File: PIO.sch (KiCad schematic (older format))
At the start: 12 parts, among them J1 Conn_02x08_Odd_Even, J2 KMDGX-6S-BS, U15 Z84C20, U16 74AHC08, U18 74HC164, U19 74HC164, U2 74AHC14

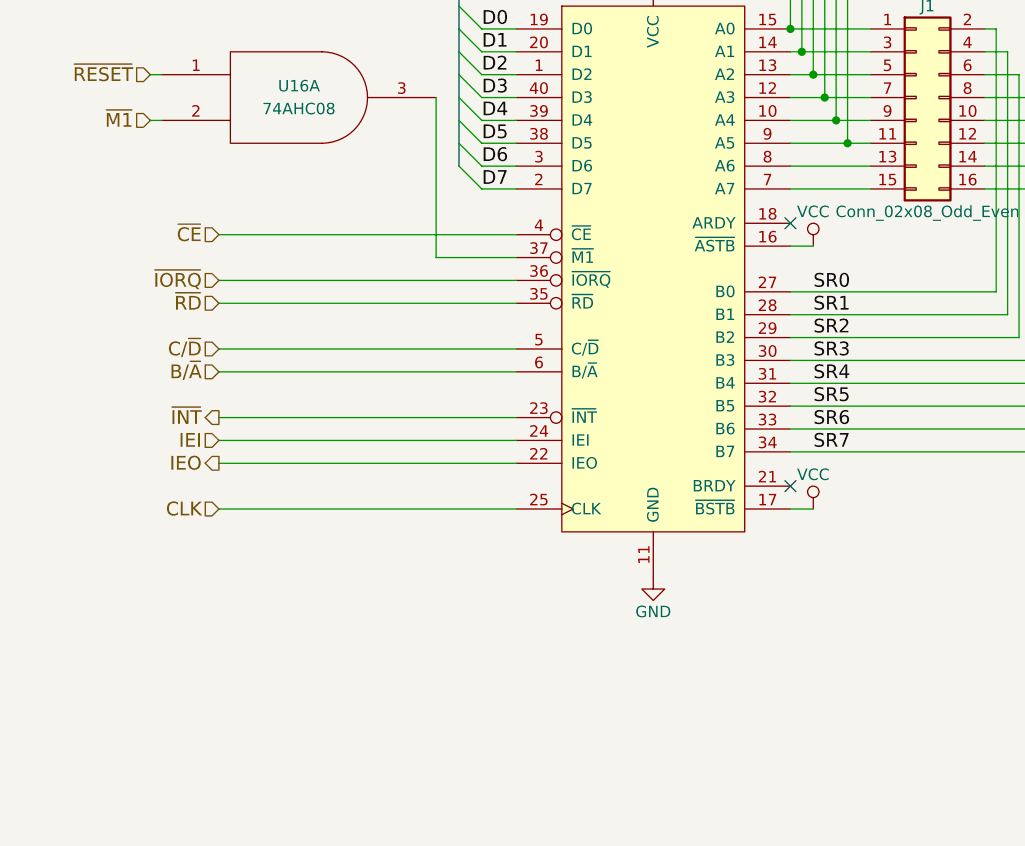
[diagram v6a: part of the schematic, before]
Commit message: Schematic for an LCD panel interface circuit.
git-svn-id: svn+ssh://dev.thehead.ca/depot/main/z80@632 995eaefb-0ce2-40e3-b8bc-69bf8729875b
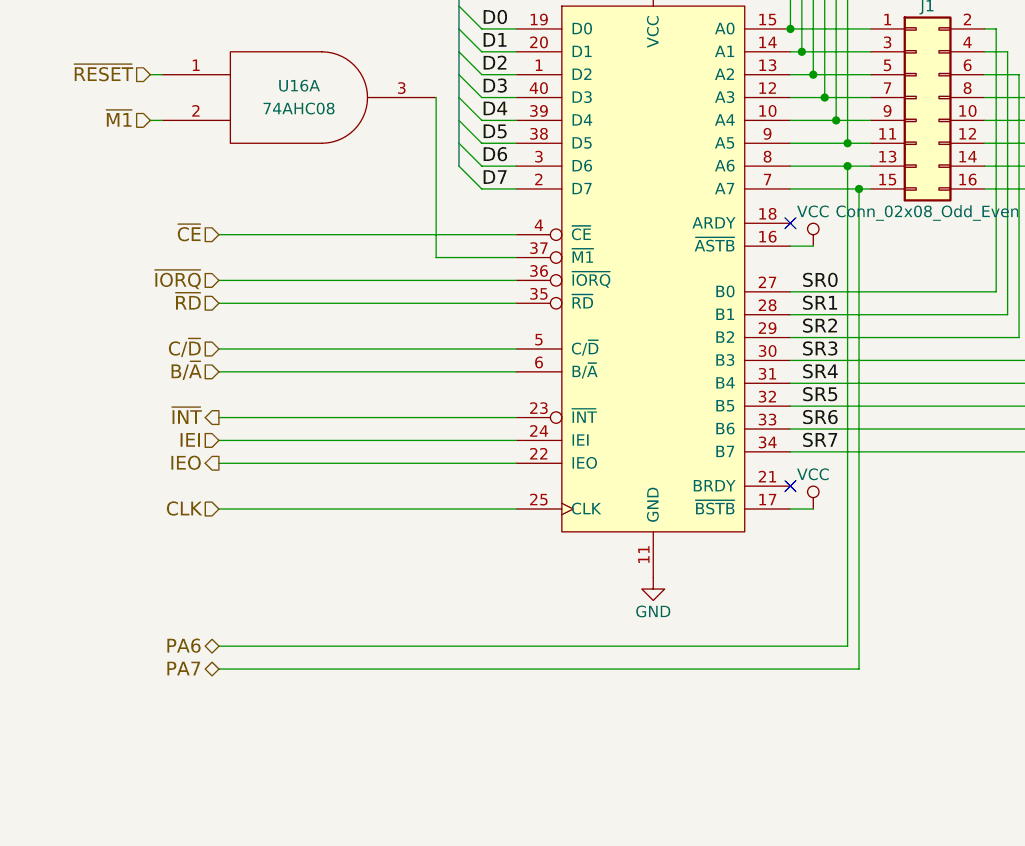
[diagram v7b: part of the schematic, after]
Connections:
- net PA7: now reaches J1.15 (Pin_15), U15.7 (A7)
- net PA6: now reaches J1.13 (Pin_13), U15.8 (A6)
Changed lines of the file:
@@
 $Descr USLetter 11000 8500
 encoding utf-8
-Sheet 5 7
+Sheet 5 8
 Title "PIO, PS/2 Keyboard Port"
-Date "2018-06-12"
-Rev "10"
+Date "2018-07-18"
+Rev "11"
 Comp ""
 Comment1 ""
@@
 ~RESET
 $Comp
-L GND #PWR055
+L GND #PWR057
 U 1 1 59D82A6F
 P 3400 4500
-F 0 "#PWR055" H 3400 4250 50  0001 C CNN
+F 0 "#PWR057" H 3400 4250 50  0001 C CNN
 F 1 "GND" H 3400 4350 50  0000 C CNN
 F 2 "" H 3400 4500 50  0001 C CNN
@@
 $EndComp
 $Comp
-L VCC #PWR056
+L VCC #PWR058
 U 1 1 59D82A86
 P 3400 1800
-F 0 "#PWR056" H 3400 1650 50  0001 C CNN
+F 0 "#PWR058" H 3400 1650 50  0001 C CNN
 F 1 "VCC" H 3400 1950 50  0000 C CNN
 F 2 "" H 3400 1800 50  0001 C CNN
@@
 NoConn ~ 4000 4100
 $Comp
-L VCC #PWR057
+L VCC #PWR059
 U 1 1 59D87E9E
 P 4100 3050
-F 0 "#PWR057" H 4100 2900 50  0001 C CNN
+F 0 "#PWR059" H 4100 2900 50  0001 C CNN
 F 1 "VCC" H 4100 3200 50  0000 C CNN
 F 2 "" H 4100 3050 50  0001 C CNN
@@
 $EndComp
 $Comp
-L VCC #PWR058
+L VCC #PWR060
 U 1 1 59D87EBB
 P 4100 4200
-F 0 "#PWR058" H 4100 4050 50  0001 C CNN
+F 0 "#PWR060" H 4100 4050 50  0001 C CNN
 F 1 "VCC" H 4100 4350 50  0000 C CNN
 F 2 "" H 4100 4200 50  0001 C CNN
@@
 	4000 3950 5250 3950
 $Comp
-L VCC #PWR059
+L VCC #PWR061
 U 1 1 59D89429
 P 9400 1200
-F 0 "#PWR059" H 9400 1050 50  0001 C CNN
+F 0 "#PWR061" H 9400 1050 50  0001 C CNN
 F 1 "VCC" H 9400 1350 50  0000 C CNN
 F 2 "" H 9400 1200 50  0001 C CNN
@@
 $EndComp
 $Comp
-L GND #PWR060
+L GND #PWR062
 U 1 1 59D8949E
 P 10200 1200
-F 0 "#PWR060" H 10200 950 50  0001 C CNN
+F 0 "#PWR062" H 10200 950 50  0001 C CNN
 F 1 "GND" H 10200 1050 50  0000 C CNN
 F 2 "" H 10200 1200 50  0001 C CNN
@@
 $EndComp
 $Comp
-L VCC #PWR061
+L VCC #PWR063
 U 1 1 59D8DE5C
 P 9650 2550
-F 0 "#PWR061" H 9650 2400 50  0001 C CNN
+F 0 "#PWR063" H 9650 2400 50  0001 C CNN
 F 1 "VCC" H 9650 2700 50  0000 C CNN
 F 2 "" H 9650 2550 50  0001 C CNN
@@
 $EndComp
 $Comp
-L VCC #PWR062
+L VCC #PWR064
 U 1 1 59D8DE9B
 P 9650 1850
-F 0 "#PWR062" H 9650 1700 50  0001 C CNN
+F 0 "#PWR064" H 9650 1700 50  0001 C CNN
 F 1 "VCC" H 9650 2000 50  0000 C CNN
 F 2 "" H 9650 1850 50  0001 C CNN
@@
 $EndComp
 $Comp
-L GND #PWR063
+L GND #PWR065
 U 1 1 59D929E0
 P 4450 6850
-F 0 "#PWR063" H 4450 6600 50  0001 C CNN
+F 0 "#PWR065" H 4450 6600 50  0001 C CNN
 F 1 "GND" H 4450 6700 50  0000 C CNN
 F 2 "" H 4450 6850 50  0001 C CNN
@@
 $EndComp
 $Comp
-L VCC #PWR064
+L VCC #PWR066
 U 1 1 59D929ED
 P 4450 6550
-F 0 "#PWR064" H 4450 6400 50  0001 C CNN
+F 0 "#PWR066" H 4450 6400 50  0001 C CNN
 F 1 "VCC" H 4450 6700 50  0000 C CNN
 F 2 "" H 4450 6550 50  0001 C CNN
@@
 Text Label 6450 3500 0    60   ~ 0
 SR0
-Text Label 4100 3250 0    60   ~ 0
+Text Label 4050 3250 0    60   ~ 0
 SR0
-Text Label 4100 3350 0    60   ~ 0
+Text Label 4050 3350 0    60   ~ 0
 SR1
-Text Label 4100 3450 0    60   ~ 0
+Text Label 4050 3450 0    60   ~ 0
 SR2
-Text Label 4100 3550 0    60   ~ 0
+Text Label 4050 3550 0    60   ~ 0
 SR3
-Text Label 4100 3650 0    60   ~ 0
+Text Label 4050 3650 0    60   ~ 0
 SR4
-Text Label 4100 3750 0    60   ~ 0
+Text Label 4050 3750 0    60   ~ 0
 SR5
-Text Label 4100 3850 0    60   ~ 0
+Text Label 4050 3850 0    60   ~ 0
 SR6
-Text Label 4100 3950 0    60   ~ 0
+Text Label 4050 3950 0    60   ~ 0
 SR7
 $Comp
@@
 $EndComp
 $Comp
-L GND #PWR065
+L GND #PWR067
 U 1 1 5AC53539
 P 9950 1650
-F 0 "#PWR065" H 9950 1400 50  0001 C CNN
+F 0 "#PWR067" H 9950 1400 50  0001 C CNN
 F 1 "GND" H 9950 1500 50  0000 C CNN
 F 2 "" H 9950 1650 50  0001 C CNN
@@
 Wire Wire Line
 	8600 850  8600 1250
+Text HLabel 1500 4800 0    60   BiDi ~ 0
+PA6
+Text HLabel 1500 4900 0    60   BiDi ~ 0
+PA7
+Wire Wire Line
+	4250 2700 4250 4800
+Wire Wire Line
+	4250 4800 1500 4800
+Connection ~ 4250 2700
+Wire Wire Line
+	4300 2800 4300 4900
+Wire Wire Line
+	4300 4900 1500 4900
+Connection ~ 4300 2800
 $EndSCHEMATC

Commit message: Latest updates; preparing to move to github (I think).
git-svn-id: svn+ssh://dev.thehead.ca/depot/main/z80@636 995eaefb-0ce2-40e3-b8bc-69bf8729875b
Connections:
- net PA6 renamed PIOA6
- net PA7 renamed PIOA7
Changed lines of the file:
@@
 $Descr USLetter 11000 8500
 encoding utf-8
-Sheet 5 8
+Sheet 5 9
 Title "PIO, PS/2 Keyboard Port"
-Date "2018-07-18"
-Rev "11"
+Date "2018-07-20"
+Rev "12"
 Comp ""
 Comment1 ""
@@
 ~RESET
 $Comp
-L GND #PWR057
+L GND #PWR055
 U 1 1 59D82A6F
 P 3400 4500
-F 0 "#PWR057" H 3400 4250 50  0001 C CNN
+F 0 "#PWR055" H 3400 4250 50  0001 C CNN
 F 1 "GND" H 3400 4350 50  0000 C CNN
 F 2 "" H 3400 4500 50  0001 C CNN
@@
 $EndComp
 $Comp
-L VCC #PWR058
+L VCC #PWR056
 U 1 1 59D82A86
 P 3400 1800
-F 0 "#PWR058" H 3400 1650 50  0001 C CNN
+F 0 "#PWR056" H 3400 1650 50  0001 C CNN
 F 1 "VCC" H 3400 1950 50  0000 C CNN
 F 2 "" H 3400 1800 50  0001 C CNN
@@
 NoConn ~ 4000 4100
 $Comp
-L VCC #PWR059
+L VCC #PWR057
 U 1 1 59D87E9E
 P 4100 3050
-F 0 "#PWR059" H 4100 2900 50  0001 C CNN
+F 0 "#PWR057" H 4100 2900 50  0001 C CNN
 F 1 "VCC" H 4100 3200 50  0000 C CNN
 F 2 "" H 4100 3050 50  0001 C CNN
@@
 $EndComp
 $Comp
-L VCC #PWR060
+L VCC #PWR058
 U 1 1 59D87EBB
 P 4100 4200
-F 0 "#PWR060" H 4100 4050 50  0001 C CNN
+F 0 "#PWR058" H 4100 4050 50  0001 C CNN
 F 1 "VCC" H 4100 4350 50  0000 C CNN
 F 2 "" H 4100 4200 50  0001 C CNN
@@
 	4000 3950 5250 3950
 $Comp
-L VCC #PWR061
+L VCC #PWR059
 U 1 1 59D89429
 P 9400 1200
-F 0 "#PWR061" H 9400 1050 50  0001 C CNN
+F 0 "#PWR059" H 9400 1050 50  0001 C CNN
 F 1 "VCC" H 9400 1350 50  0000 C CNN
 F 2 "" H 9400 1200 50  0001 C CNN
@@
 $EndComp
 $Comp
-L GND #PWR062
+L GND #PWR060
 U 1 1 59D8949E
 P 10200 1200
-F 0 "#PWR062" H 10200 950 50  0001 C CNN
+F 0 "#PWR060" H 10200 950 50  0001 C CNN
 F 1 "GND" H 10200 1050 50  0000 C CNN
 F 2 "" H 10200 1200 50  0001 C CNN
@@
 $EndComp
 $Comp
-L VCC #PWR063
+L VCC #PWR061
 U 1 1 59D8DE5C
 P 9650 2550
-F 0 "#PWR063" H 9650 2400 50  0001 C CNN
+F 0 "#PWR061" H 9650 2400 50  0001 C CNN
 F 1 "VCC" H 9650 2700 50  0000 C CNN
 F 2 "" H 9650 2550 50  0001 C CNN
@@
 $EndComp
 $Comp
-L VCC #PWR064
+L VCC #PWR062
 U 1 1 59D8DE9B
 P 9650 1850
-F 0 "#PWR064" H 9650 1700 50  0001 C CNN
+F 0 "#PWR062" H 9650 1700 50  0001 C CNN
 F 1 "VCC" H 9650 2000 50  0000 C CNN
 F 2 "" H 9650 1850 50  0001 C CNN
@@
 $EndComp
 $Comp
-L GND #PWR065
+L GND #PWR063
 U 1 1 59D929E0
 P 4450 6850
-F 0 "#PWR065" H 4450 6600 50  0001 C CNN
+F 0 "#PWR063" H 4450 6600 50  0001 C CNN
 F 1 "GND" H 4450 6700 50  0000 C CNN
 F 2 "" H 4450 6850 50  0001 C CNN
@@
 $EndComp
 $Comp
-L VCC #PWR066
+L VCC #PWR064
 U 1 1 59D929ED
 P 4450 6550
-F 0 "#PWR066" H 4450 6400 50  0001 C CNN
+F 0 "#PWR064" H 4450 6400 50  0001 C CNN
 F 1 "VCC" H 4450 6700 50  0000 C CNN
 F 2 "" H 4450 6550 50  0001 C CNN
@@
 $EndComp
 $Comp
-L GND #PWR067
+L GND #PWR065
 U 1 1 5AC53539
 P 9950 1650
-F 0 "#PWR067" H 9950 1400 50  0001 C CNN
+F 0 "#PWR065" H 9950 1400 50  0001 C CNN
 F 1 "GND" H 9950 1500 50  0000 C CNN
 F 2 "" H 9950 1650 50  0001 C CNN
@@
 	8600 850  8600 1250
 Text HLabel 1500 4800 0    60   BiDi ~ 0
-PA6
+PIOA6
 Text HLabel 1500 4900 0    60   BiDi ~ 0
-PA7
+PIOA7
 Wire Wire Line
 	4250 2700 4250 4800
